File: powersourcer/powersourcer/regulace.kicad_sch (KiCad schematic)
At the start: 39 parts, among them Q1 2N2222, Q10 TIP35C, Q2 TIP122, Q3 TIP35C, Q4 TIP35C, Q5 TIP35C, Q6 TIP35C, Q7 TIP35C, Q8 TIP35C, Q9 TIP35C, U1 LM336Z-5.0, U2 TL081

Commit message: poslední práce.
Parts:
- renumbered H5 to H3, H6 to H4, H3 to H5, H4 to H6
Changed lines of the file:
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@@
 		(dnp no)
 		(fields_autoplaced yes)
-		(property "Reference" "#PWR03"
+		(property "Reference" "#PWR01"
 			(at 262.89 25.4 0)
 			(hide yes)
@@
 			(project "powersourcer"
 				(path "/3b543968-b752-41ec-9e14-3a471f109ffc/57492013-ce66-4b1a-aeb4-b7d85251d918"
-					(reference "#PWR03")
+					(reference "#PWR01")
 					(unit 1)
 				)
@@
 		(in_pos_files yes)
 		(dnp no)
-		(property "Reference" "#PWR04"
+		(property "Reference" "#PWR02"
 			(at 262.89 48.26 0)
 			(hide yes)
@@
 			(project "powersourcer"
 				(path "/3b543968-b752-41ec-9e14-3a471f109ffc/57492013-ce66-4b1a-aeb4-b7d85251d918"
-					(reference "#PWR04")
+					(reference "#PWR02")
 					(unit 1)
 				)
@@
 		(dnp no)
 		(fields_autoplaced yes)
-		(property "Reference" "H4"
+		(property "Reference" "H6"
 			(at 273.05 38.0999 90)
 			(show_name no)
@@
 			(project "powersourcer"
 				(path "/3b543968-b752-41ec-9e14-3a471f109ffc/57492013-ce66-4b1a-aeb4-b7d85251d918"
-					(reference "H4")
+					(reference "H6")
 					(unit 1)
 				)
@@
 		(dnp no)
 		(fields_autoplaced yes)
-		(property "Reference" "H6"
+		(property "Reference" "H4"
 			(at 116.84 40.6399 90)
 			(show_name no)
@@
 			(project "powersourcer"
 				(path "/3b543968-b752-41ec-9e14-3a471f109ffc/57492013-ce66-4b1a-aeb4-b7d85251d918"
-					(reference "H6")
+					(reference "H4")
 					(unit 1)
 				)
@@
 		(dnp no)
 		(fields_autoplaced yes)
-		(property "Reference" "H3"
+		(property "Reference" "H5"
 			(at 273.05 22.8599 90)
 			(show_name no)
@@
 			(project "powersourcer"
 				(path "/3b543968-b752-41ec-9e14-3a471f109ffc/57492013-ce66-4b1a-aeb4-b7d85251d918"
-					(reference "H3")
+					(reference "H5")
 					(unit 1)
 				)
@@
 		(dnp no)
 		(fields_autoplaced yes)
-		(property "Reference" "H5"
+		(property "Reference" "H3"
 			(at 116.84 27.9399 90)
 			(show_name no)
@@
 			(project "powersourcer"
 				(path "/3b543968-b752-41ec-9e14-3a471f109ffc/57492013-ce66-4b1a-aeb4-b7d85251d918"
-					(reference "H5")
+					(reference "H3")
 					(unit 1)
 				)

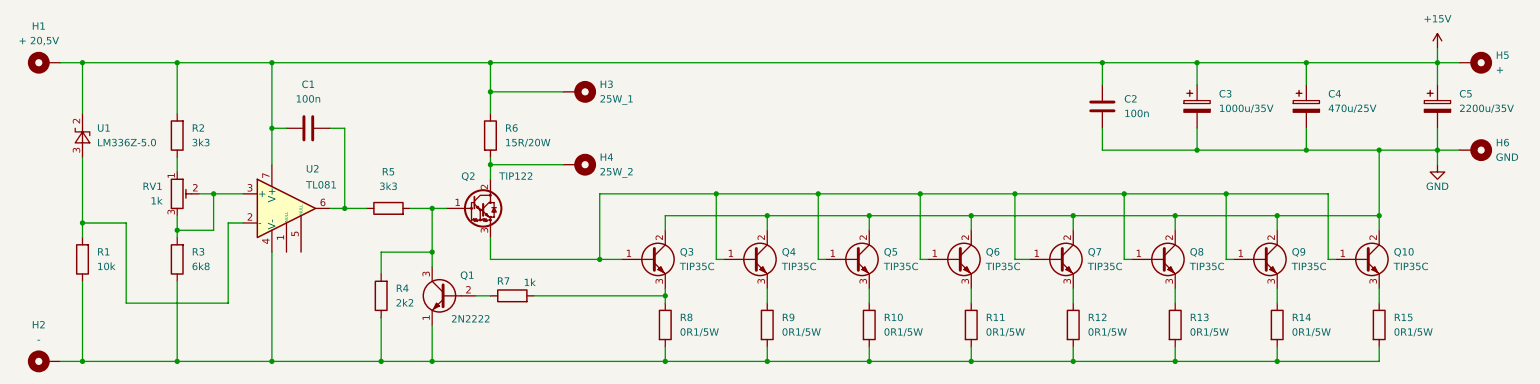
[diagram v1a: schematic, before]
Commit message: Doplněny bázové odpory silových tranzistorů.
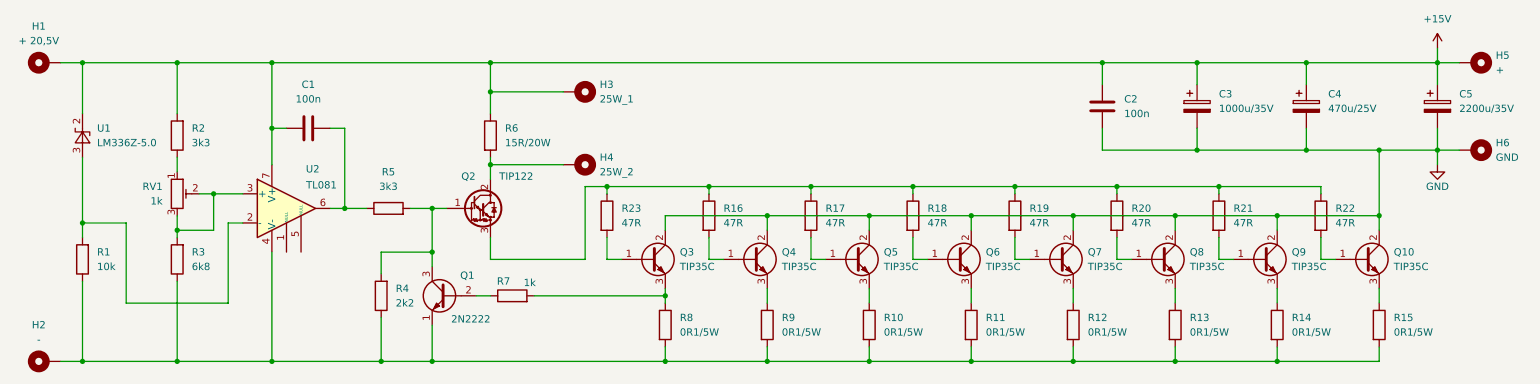
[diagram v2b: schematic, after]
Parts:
- added R16, R17, R18, R19, R20, R21, R22, R23: 47R, symbol Device:R
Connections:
- new net: Q2.3 (E), R16.1, R17.1, R18.1, R19.1, R20.1, R21.1, R22.1, R23.1
- new net: Q7.1 (B), R19.2
- new net: Q3.1 (B), R23.2
- new net: Q5.1 (B), R17.2
- new net: Q8.1 (B), R20.2
- new net: Q9.1 (B), R21.2
- new net: Q4.1 (B), R16.2
- new net: Q10.1 (B), R22.2
- new net: Q6.1 (B), R18.2

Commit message: Přečíslování součástek před přiřazením pouzder.
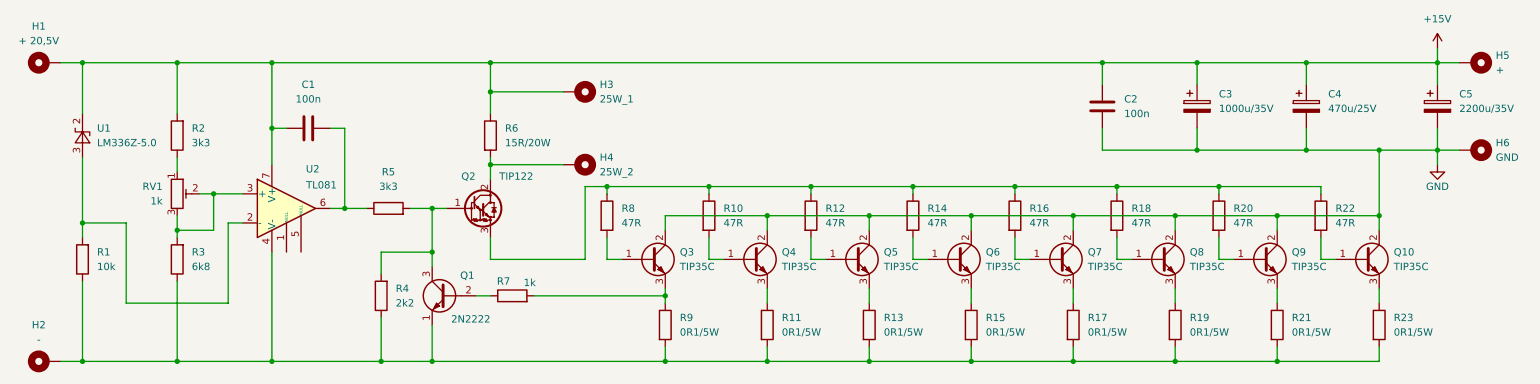
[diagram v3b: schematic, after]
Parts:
- renumbered R16 to R10, R9 to R11, R17 to R12, R10 to R13, R18 to R14, R11 to R15, R19 to R16, R12 to R17, R20 to R18, R13 to R19, R21 to R20, R14 to R21, R15 to R23, R23 to R8, R8 to R9
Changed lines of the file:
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@@
 		(dnp no)
 		(fields_autoplaced yes)
-		(property "Reference" "R8"
+		(property "Reference" "R9"
 			(at 130.81 68.5799 0)
 			(show_name no)
@@
 			(project "powersourcer"
 				(path "/3b543968-b752-41ec-9e14-3a471f109ffc/57492013-ce66-4b1a-aeb4-b7d85251d918"
-					(reference "R8")
+					(reference "R9")
 					(unit 1)
 				)
@@
 		(dnp no)
 		(fields_autoplaced yes)
-		(property "Reference" "R19"
+		(property "Reference" "R16"
 			(at 191.77 49.5299 0)
 			(show_name no)
@@
 			(project "powersourcer"
 				(path "/3b543968-b752-41ec-9e14-3a471f109ffc/57492013-ce66-4b1a-aeb4-b7d85251d918"
-					(reference "R19")
+					(reference "R16")
 					(unit 1)
 				)
@@
 		(dnp no)
 		(fields_autoplaced yes)
-		(property "Reference" "R10"
+		(property "Reference" "R13"
 			(at 166.37 68.5799 0)
 			(show_name no)
@@
 			(project "powersourcer"
 				(path "/3b543968-b752-41ec-9e14-3a471f109ffc/57492013-ce66-4b1a-aeb4-b7d85251d918"
-					(reference "R10")
+					(reference "R13")
 					(unit 1)
 				)
@@
 		(dnp no)
 		(fields_autoplaced yes)
-		(property "Reference" "R23"
+		(property "Reference" "R8"
 			(at 120.65 49.5299 0)
 			(show_name no)
@@
 			(project "powersourcer"
 				(path "/3b543968-b752-41ec-9e14-3a471f109ffc/57492013-ce66-4b1a-aeb4-b7d85251d918"
-					(reference "R23")
+					(reference "R8")
 					(unit 1)
 				)
@@
 		(dnp no)
 		(fields_autoplaced yes)
-		(property "Reference" "R17"
+		(property "Reference" "R12"
 			(at 156.21 49.5299 0)
 			(show_name no)
@@
 			(project "powersourcer"
 				(path "/3b543968-b752-41ec-9e14-3a471f109ffc/57492013-ce66-4b1a-aeb4-b7d85251d918"
-					(reference "R17")
+					(reference "R12")
 					(unit 1)
 				)
@@
 		(dnp no)
 		(fields_autoplaced yes)
-		(property "Reference" "R20"
+		(property "Reference" "R18"
 			(at 209.55 49.5299 0)
 			(show_name no)
@@
 			(project "powersourcer"
 				(path "/3b543968-b752-41ec-9e14-3a471f109ffc/57492013-ce66-4b1a-aeb4-b7d85251d918"
-					(reference "R20")
+					(reference "R18")
 					(unit 1)
 				)
@@
 		(dnp no)
 		(fields_autoplaced yes)
-		(property "Reference" "R16"
+		(property "Reference" "R10"
 			(at 138.43 49.5299 0)
 			(show_name no)
@@
 			(project "powersourcer"
 				(path "/3b543968-b752-41ec-9e14-3a471f109ffc/57492013-ce66-4b1a-aeb4-b7d85251d918"
-					(reference "R16")
+					(reference "R10")
 					(unit 1)
 				)
@@
 		(dnp no)
 		(fields_autoplaced yes)
-		(property "Reference" "R9"
+		(property "Reference" "R11"
 			(at 148.59 68.5799 0)
 			(show_name no)
@@
 			(project "powersourcer"
 				(path "/3b543968-b752-41ec-9e14-3a471f109ffc/57492013-ce66-4b1a-aeb4-b7d85251d918"
-					(reference "R9")
+					(reference "R11")
 					(unit 1)
 				)
@@
 		(dnp no)
 		(fields_autoplaced yes)
-		(property "Reference" "R13"
+		(property "Reference" "R19"
 			(at 219.71 68.5799 0)
 			(show_name no)
@@
 			(project "powersourcer"
 				(path "/3b543968-b752-41ec-9e14-3a471f109ffc/57492013-ce66-4b1a-aeb4-b7d85251d918"
-					(reference "R13")
+					(reference "R19")
 					(unit 1)
 				)
@@
 		(dnp no)
 		(fields_autoplaced yes)
-		(property "Reference" "R14"
+		(property "Reference" "R21"
 			(at 237.49 68.5799 0)
 			(show_name no)
@@
 			(project "powersourcer"
 				(path "/3b543968-b752-41ec-9e14-3a471f109ffc/57492013-ce66-4b1a-aeb4-b7d85251d918"
-					(reference "R14")
+					(reference "R21")
 					(unit 1)
 				)
@@
 		(dnp no)
 		(fields_autoplaced yes)
-		(property "Reference" "R12"
+		(property "Reference" "R17"
 			(at 201.93 68.5799 0)
 			(show_name no)
@@
 			(project "powersourcer"
 				(path "/3b543968-b752-41ec-9e14-3a471f109ffc/57492013-ce66-4b1a-aeb4-b7d85251d918"
-					(reference "R12")
+					(reference "R17")
 					(unit 1)
 				)
@@
 		(dnp no)
 		(fields_autoplaced yes)
-		(property "Reference" "R18"
+		(property "Reference" "R14"
 			(at 173.99 49.5299 0)
 			(show_name no)
@@
 			(project "powersourcer"
 				(path "/3b543968-b752-41ec-9e14-3a471f109ffc/57492013-ce66-4b1a-aeb4-b7d85251d918"
-					(reference "R18")
+					(reference "R14")
 					(unit 1)
 				)
@@
 		(dnp no)
 		(fields_autoplaced yes)
-		(property "Reference" "R15"
+		(property "Reference" "R23"
 			(at 255.27 68.5799 0)
 			(show_name no)
@@
 			(project "powersourcer"
 				(path "/3b543968-b752-41ec-9e14-3a471f109ffc/57492013-ce66-4b1a-aeb4-b7d85251d918"
-					(reference "R15")
+					(reference "R23")
 					(unit 1)
 				)
@@
 		(dnp no)
 		(fields_autoplaced yes)
-		(property "Reference" "R11"
+		(property "Reference" "R15"
 			(at 184.15 68.5799 0)
 			(show_name no)
@@
 			(project "powersourcer"
 				(path "/3b543968-b752-41ec-9e14-3a471f109ffc/57492013-ce66-4b1a-aeb4-b7d85251d918"
-					(reference "R11")
+					(reference "R15")
 					(unit 1)
 				)
@@
 		(dnp no)
 		(fields_autoplaced yes)
-		(property "Reference" "R21"
+		(property "Reference" "R20"
 			(at 227.33 49.5299 0)
 			(show_name no)
@@
 			(project "powersourcer"
 				(path "/3b543968-b752-41ec-9e14-3a471f109ffc/57492013-ce66-4b1a-aeb4-b7d85251d918"
-					(reference "R21")
+					(reference "R20")
 					(unit 1)
 				)

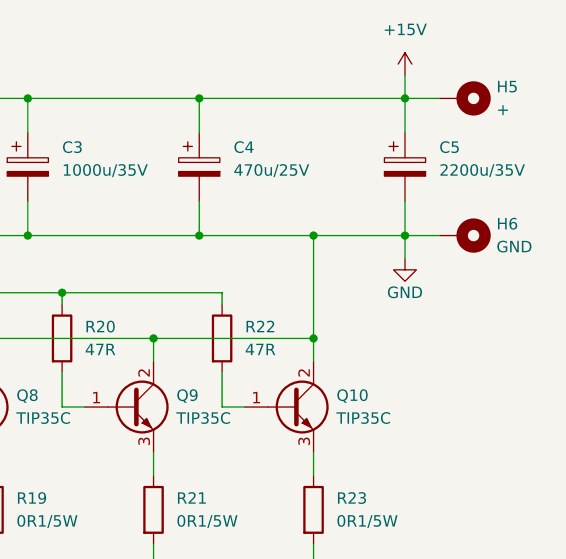
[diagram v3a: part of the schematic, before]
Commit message: Přiřazení pouzder.
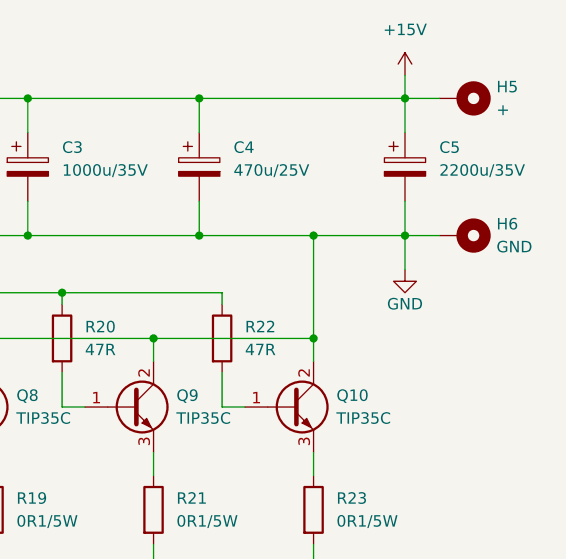
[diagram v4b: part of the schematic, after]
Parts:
- Q10, Q3, Q4, Q5, Q6, Q7, Q8, Q9: footprint Package_TO_SOT_THT:TO-247-3_Vertical -> HAM_Lib:TO-247-3_Vertical
- Q2: footprint Package_TO_SOT_THT:TO-220-3_Vertical -> HAM_Lib:TO-247-3_Vertical
- R1, R2, R3, R4, R5, R7: footprint (none) -> Resistor_SMD:R_1206_3216Metric_Pad1.30x1.75mm_HandSolder
- R10, R12, R14, R16, R18, R20, R22, R8: footprint (none) -> HAM_Lib:R_Axial_DIN0309_L9.0mm_D3.2mm_P12.70mm_Horizontal
- R11, R13, R15, R17, R19, R21, R23, R9: footprint (none) -> HAM_Lib:R_Radial_Power_L13.0mm_W9.0mm_P5.00mm
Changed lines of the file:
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@@
 	(wire
 		(pts
-			(xy 262.89 39.37) (xy 262.89 41.91)
+			(xy 262.89 39.37) (xy 262.89 43.18)
 		)
 		(stroke
@@
 			)
 		)
-		(property "Footprint" ""
+		(property "Footprint" "Resistor_SMD:R_1206_3216Metric_Pad1.30x1.75mm_HandSolder"
 			(at 44.958 36.83 90)
 			(hide yes)
@@
 			)
 		)
-		(property "Footprint" ""
+		(property "Footprint" "HAM_Lib:R_Radial_Power_L13.0mm_W9.0mm_P5.00mm"
 			(at 126.492 69.85 90)
 			(hide yes)
@@
 			)
 		)
-		(property "Footprint" ""
+		(property "Footprint" "HAM_Lib:R_Axial_DIN0309_L9.0mm_D3.2mm_P12.70mm_Horizontal"
 			(at 187.452 50.8 90)
 			(hide yes)
@@
 			)
 		)
-		(property "Footprint" ""
+		(property "Footprint" "HAM_Lib:R_Radial_Power_L13.0mm_W9.0mm_P5.00mm"
 			(at 162.052 69.85 90)
 			(hide yes)
@@
 			)
 		)
-		(property "Footprint" ""
+		(property "Footprint" "HAM_Lib:R_Axial_DIN0309_L9.0mm_D3.2mm_P12.70mm_Horizontal"
 			(at 116.332 50.8 90)
 			(hide yes)
@@
 	(symbol
 		(lib_id "power:GND")
-		(at 262.89 41.91 0)
+		(at 262.89 43.18 0)
 		(unit 1)
 		(body_style 1)
@@
 		(dnp no)
 		(property "Reference" "#PWR02"
-			(at 262.89 48.26 0)
+			(at 262.89 49.53 0)
 			(hide yes)
 			(show_name no)
@@
 		)
 		(property "Value" "GND"
-			(at 262.89 45.72 0)
+			(at 262.89 46.99 0)
 			(show_name no)
 			(do_not_autoplace no)
@@
 		)
 		(property "Footprint" ""
-			(at 262.89 41.91 0)
+			(at 262.89 43.18 0)
 			(hide yes)
 			(show_name no)
@@
 		)
 		(property "Datasheet" ""
-			(at 262.89 41.91 0)
+			(at 262.89 43.18 0)
 			(hide yes)
 			(show_name no)
@@
 		)
 		(property "Description" "Power symbol creates a global label with name \"GND\" , ground"
-			(at 262.89 41.91 0)
+			(at 262.89 43.18 0)
 			(hide yes)
 			(show_name no)
@@
 			)
 		)
-		(property "Footprint" ""
+		(property "Footprint" "Resistor_SMD:R_1206_3216Metric_Pad1.30x1.75mm_HandSolder"
 			(at 80.01 51.308 90)
 			(hide yes)
@@
 			)
 		)
-		(property "Footprint" ""
+		(property "Footprint" "HAM_Lib:R_Axial_DIN0309_L9.0mm_D3.2mm_P12.70mm_Horizontal"
 			(at 151.892 50.8 90)
 			(hide yes)
@@
 			)
 		)
-		(property "Footprint" ""
+		(property "Footprint" "HAM_Lib:R_Axial_DIN0309_L9.0mm_D3.2mm_P12.70mm_Horizontal"
 			(at 205.232 50.8 90)
 			(hide yes)
@@
 			)
 		)
-		(property "Footprint" "Package_TO_SOT_THT:TO-247-3_Vertical"
+		(property "Footprint" "HAM_Lib:TO-247-3_Vertical"
 			(at 237.49 60.325 0)
 			(hide yes)
@@
 			)
 		)
-		(property "Footprint" ""
+		(property "Footprint" "HAM_Lib:R_Axial_DIN0309_L9.0mm_D3.2mm_P12.70mm_Horizontal"
 			(at 134.112 50.8 90)
 			(hide yes)
@@
 			)
 		)
-		(property "Footprint" "Package_TO_SOT_THT:TO-220-3_Vertical"
+		(property "Footprint" "HAM_Lib:TO-247-3_Vertical"
 			(at 100.33 51.435 0)
 			(hide yes)
@@
 			)
 		)
-		(property "Footprint" "Package_TO_SOT_THT:TO-247-3_Vertical"
+		(property "Footprint" "HAM_Lib:TO-247-3_Vertical"
 			(at 219.71 60.325 0)
 			(hide yes)
@@
 			)
 		)
-		(property "Footprint" ""
+		(property "Footprint" "HAM_Lib:R_Radial_Power_L13.0mm_W9.0mm_P5.00mm"
 			(at 144.272 69.85 90)
 			(hide yes)
@@
 			)
 		)
-		(property "Footprint" ""
+		(property "Footprint" "HAM_Lib:R_Radial_Power_L13.0mm_W9.0mm_P5.00mm"
 			(at 215.392 69.85 90)
 			(hide yes)
@@
 			)
 		)
-		(property "Footprint" "Package_TO_SOT_THT:TO-247-3_Vertical"
+		(property "Footprint" "HAM_Lib:TO-247-3_Vertical"
 			(at 201.93 60.325 0)
 			(hide yes)
@@
 			)
 		)
-		(property "Footprint" ""
+		(property "Footprint" "HAM_Lib:R_Radial_Power_L13.0mm_W9.0mm_P5.00mm"
 			(at 233.172 69.85 90)
 			(hide yes)
@@
 			)
 		)
-		(property "Footprint" ""
+		(property "Footprint" "HAM_Lib:R_Radial_Power_L13.0mm_W9.0mm_P5.00mm"
 			(at 197.612 69.85 90)
 			(hide yes)
@@
 			)
 		)
-		(property "Footprint" ""
+		(property "Footprint" "Resistor_SMD:R_1206_3216Metric_Pad1.30x1.75mm_HandSolder"
 			(at 80.518 64.77 90)
 			(hide yes)
@@
 			)
 		)
-		(property "Footprint" "Package_TO_SOT_THT:TO-247-3_Vertical"
+		(property "Footprint" "HAM_Lib:TO-247-3_Vertical"
 			(at 166.37 60.325 0)
 			(hide yes)
@@
 			)
 		)
-		(property "Footprint" "Package_TO_SOT_THT:TO-247-3_Vertical"
+		(property "Footprint" "HAM_Lib:TO-247-3_Vertical"
 			(at 255.27 60.325 0)
 			(hide yes)
@@
 			)
 		)
-		(property "Footprint" ""
+		(property "Footprint" "Resistor_SMD:R_1206_3216Metric_Pad1.30x1.75mm_HandSolder"
 			(at 28.448 58.42 90)
 			(hide yes)
@@
 			)
 		)
-		(property "Footprint" ""
+		(property "Footprint" "HAM_Lib:R_Axial_DIN0309_L9.0mm_D3.2mm_P12.70mm_Horizontal"
 			(at 169.672 50.8 90)
 			(hide yes)
@@
 			)
 		)
-		(property "Footprint" ""
+		(property "Footprint" "HAM_Lib:R_Radial_Power_L13.0mm_W9.0mm_P5.00mm"
 			(at 250.952 69.85 90)
 			(hide yes)
@@
 			)
 		)
-		(property "Footprint" ""
+		(property "Footprint" "Resistor_SMD:R_1206_3216Metric_Pad1.30x1.75mm_HandSolder"
 			(at 44.958 58.42 90)
 			(hide yes)
@@
 			)
 		)
-		(property "Footprint" "Package_TO_SOT_THT:TO-247-3_Vertical"
+		(property "Footprint" "HAM_Lib:TO-247-3_Vertical"
 			(at 148.59 60.325 0)
 			(hide yes)
@@
 			)
 		)
-		(property "Footprint" ""
+		(property "Footprint" "Resistor_SMD:R_1206_3216Metric_Pad1.30x1.75mm_HandSolder"
 			(at 101.6 66.548 90)
 			(hide yes)
@@
 			)
 		)
-		(property "Footprint" ""
+		(property "Footprint" "HAM_Lib:R_Radial_Power_L13.0mm_W9.0mm_P5.00mm"
 			(at 179.832 69.85 90)
 			(hide yes)
@@
 			)
 		)
-		(property "Footprint" "Package_TO_SOT_THT:TO-247-3_Vertical"
+		(property "Footprint" "HAM_Lib:TO-247-3_Vertical"
 			(at 184.15 60.325 0)
 			(hide yes)
@@
 			)
 		)
-		(property "Footprint" "Package_TO_SOT_THT:TO-247-3_Vertical"
+		(property "Footprint" "HAM_Lib:TO-247-3_Vertical"
 			(at 130.81 60.325 0)
 			(hide yes)
@@
 			)
 		)
-		(property "Footprint" ""
+		(property "Footprint" "HAM_Lib:R_Axial_DIN0309_L9.0mm_D3.2mm_P12.70mm_Horizontal"
 			(at 223.012 50.8 90)
 			(hide yes)
@@
 			)
 		)
-		(property "Footprint" ""
+		(property "Footprint" "HAM_Lib:R_Axial_DIN0309_L9.0mm_D3.2mm_P12.70mm_Horizontal"
 			(at 240.792 50.8 90)
 			(hide yes)
